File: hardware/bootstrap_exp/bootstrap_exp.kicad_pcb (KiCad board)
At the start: 4 copper layers, 86.4 x 40.6 mm, 32 parts, among them J1 Conn_Coaxial, J2 Conn_01x01, J3 Conn_01x03, J4 Conn_01x03, J5 Conn_Coaxial, U1 OPA810DBV, U2 OPA810DBV, U3 OPA810DBV

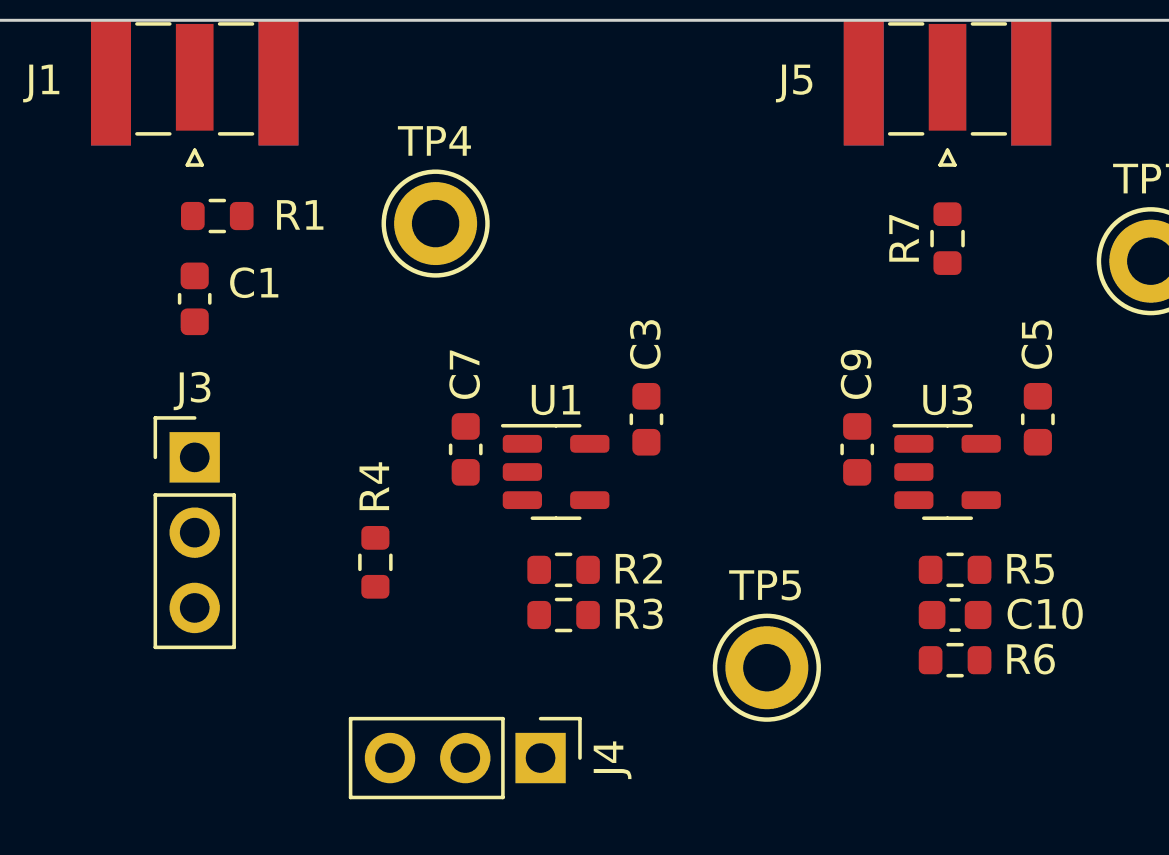
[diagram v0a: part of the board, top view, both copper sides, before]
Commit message: Setup physical stackup and design rules
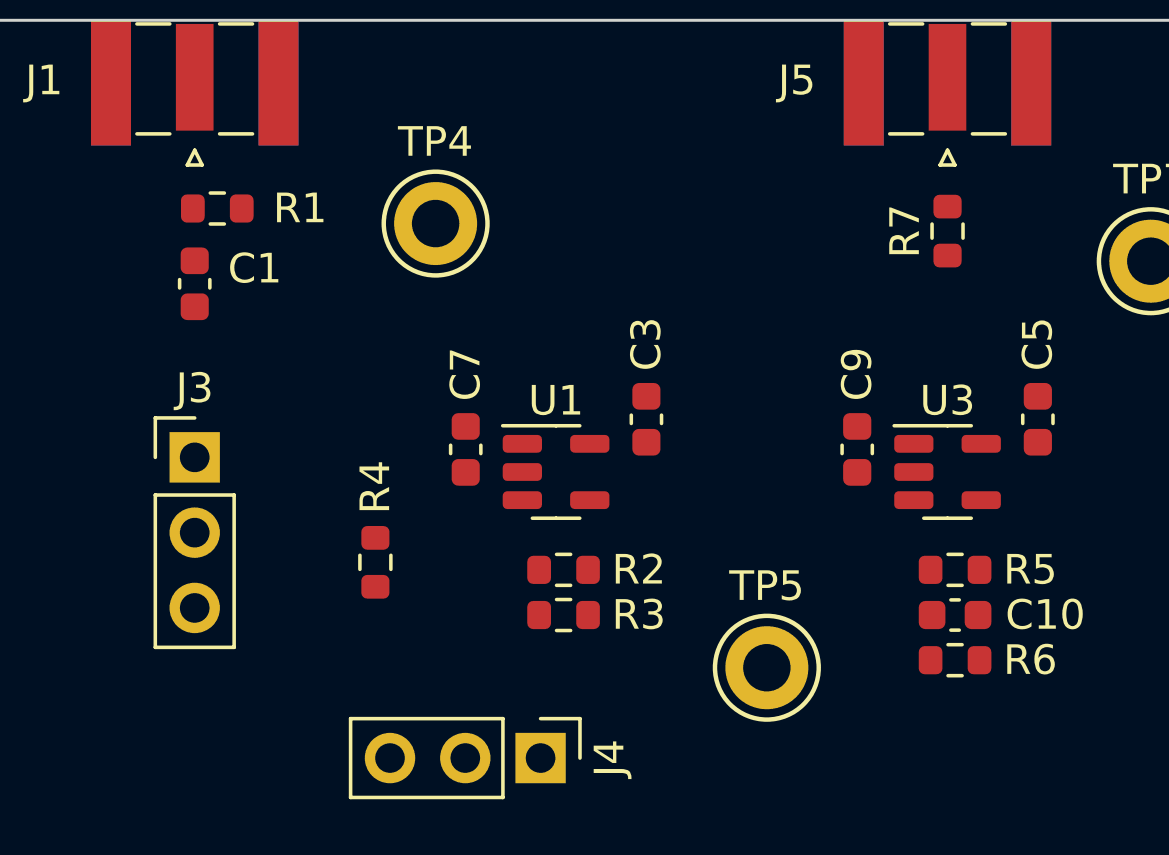
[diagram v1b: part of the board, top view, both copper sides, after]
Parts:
- moved C1 0.51 mm to (129.5, 85.1)
- moved R1 0.25 mm to (130.3, 82.5)
- moved R7 0.25 mm to (154.9, 83.3)
- turned R6 to 180 degrees
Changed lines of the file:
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@@
 (kicad_pcb (version 20211014) (generator pcbnew)
   (general
-    (thickness 4.69)
+    (thickness 1.59)
   )
   (paper "A4")
@@
       (layer "F.Mask" (type "Top Solder Mask") (thickness 0.01))
       (layer "F.Cu" (type "copper") (thickness 0.035))
-      (layer "dielectric 1" (type "core") (thickness 1.51) (material "FR4") (epsilon_r 4.5) (loss_tangent 0.02))
-      (layer "In1.Cu" (type "copper") (thickness 0.035))
-      (layer "dielectric 2" (type "prepreg") (thickness 1.51) (material "FR4") (epsilon_r 4.5) (loss_tangent 0.02))
-      (layer "In2.Cu" (type "copper") (thickness 0.035))
-      (layer "dielectric 3" (type "core") (thickness 1.51) (material "FR4") (epsilon_r 4.5) (loss_tangent 0.02))
+      (layer "dielectric 1" (type "core") (thickness 0.1) (material "FR4") (epsilon_r 4.05) (loss_tangent 0.02))
+      (layer "In1.Cu" (type "copper") (thickness 0.0175))
+      (layer "dielectric 2" (type "prepreg") (thickness 1.265) (material "FR4") (epsilon_r 4.6) (loss_tangent 0.02))
+      (layer "In2.Cu" (type "copper") (thickness 0.0175))
+      (layer "dielectric 3" (type "core") (thickness 0.1) (material "FR4") (epsilon_r 4.05) (loss_tangent 0.02))
       (layer "B.Cu" (type "copper") (thickness 0.035))
       (layer "B.Mask" (type "Bottom Solder Mask") (thickness 0.01))
@@
       (layer "B.SilkS" (type "Bottom Silk Screen"))
       (copper_finish "None")
-      (dielectric_constraints no)
+      (dielectric_constraints yes)
     )
     (pad_to_mask_clearance 0)
@@
   )
   (footprint "Resistor_SMD:R_0603_1608Metric" (layer "F.Cu")
-    (at 155.194 97.79)
+    (at 155.194 97.79 180)
     (descr "Resistor SMD 0603 (1608 Metric), square (rectangular) end terminal, IPC_7351 nominal, (Body size source: IPC-SM-782 page 72, https://www.pcb-3d.com/wordpress/wp-content/uploads/ipc-sm-782a_amendment_1_and_2.pdf), generated with kicad-footprint-generator")
     (tags "resistor")
@@
     (property "Sheetname" "")
     (attr smd)
-    (fp_text reference "R6" (at 2.54 0) (layer "F.SilkS")
+    (fp_text reference "R6" (at -2.54 0) (layer "F.SilkS")
       (effects (font (size 1 1) (thickness 0.15)))
     )
@@
     (fp_line (start 0.8 0.4125) (end -0.8 0.4125) (layer "F.Fab") (width 0.1))
     (fp_line (start -0.8 0.4125) (end -0.8 -0.4125) (layer "F.Fab") (width 0.1))
-    (pad "1" smd roundrect (at -0.825 0) (size 0.8 0.95) (layers "F.Cu" "F.Paste" "F.Mask") (roundrect_rratio 0.25)
+    (pad "1" smd roundrect (at -0.825 0 180) (size 0.8 0.95) (layers "F.Cu" "F.Paste" "F.Mask") (roundrect_rratio 0.25)
       (net 7 "Net-(C10-Pad2)") (pintype "passive"))
-    (pad "2" smd roundrect (at 0.825 0) (size 0.8 0.95) (layers "F.Cu" "F.Paste" "F.Mask") (roundrect_rratio 0.25)
+    (pad "2" smd roundrect (at 0.825 0 180) (size 0.8 0.95) (layers "F.Cu" "F.Paste" "F.Mask") (roundrect_rratio 0.25)
       (net 4 "GND") (pintype "passive"))
     (model "${KICAD6_3DMODEL_DIR}/Resistor_SMD.3dshapes/R_0603_1608Metric.wrl"
@@
   )
   (footprint "Resistor_SMD:R_0603_1608Metric" (layer "F.Cu")
-    (at 130.302 82.804)
+    (at 130.302 82.55)
     (descr "Resistor SMD 0603 (1608 Metric), square (rectangular) end terminal, IPC_7351 nominal, (Body size source: IPC-SM-782 page 72, https://www.pcb-3d.com/wordpress/wp-content/uploads/ipc-sm-782a_amendment_1_and_2.pdf), generated with kicad-footprint-generator")
     (tags "resistor")
@@
   )
   (footprint "Capacitor_SMD:C_0603_1608Metric" (layer "F.Cu")
-    (at 129.54 85.598 90)
+    (at 129.54 85.09 90)
     (descr "Capacitor SMD 0603 (1608 Metric), square (rectangular) end terminal, IPC_7351 nominal, (Body size source: IPC-SM-782 page 76, https://www.pcb-3d.com/wordpress/wp-content/uploads/ipc-sm-782a_amendment_1_and_2.pdf), generated with kicad-footprint-generator")
     (tags "capacitor")
@@
   )
   (footprint "Resistor_SMD:R_0603_1608Metric" (layer "F.Cu")
-    (at 154.94 83.566 90)
+    (at 154.94 83.312 90)
     (descr "Resistor SMD 0603 (1608 Metric), square (rectangular) end terminal, IPC_7351 nominal, (Body size source: IPC-SM-782 page 72, https://www.pcb-3d.com/wordpress/wp-content/uploads/ipc-sm-782a_amendment_1_and_2.pdf), generated with kicad-footprint-generator")
     (tags "resistor")

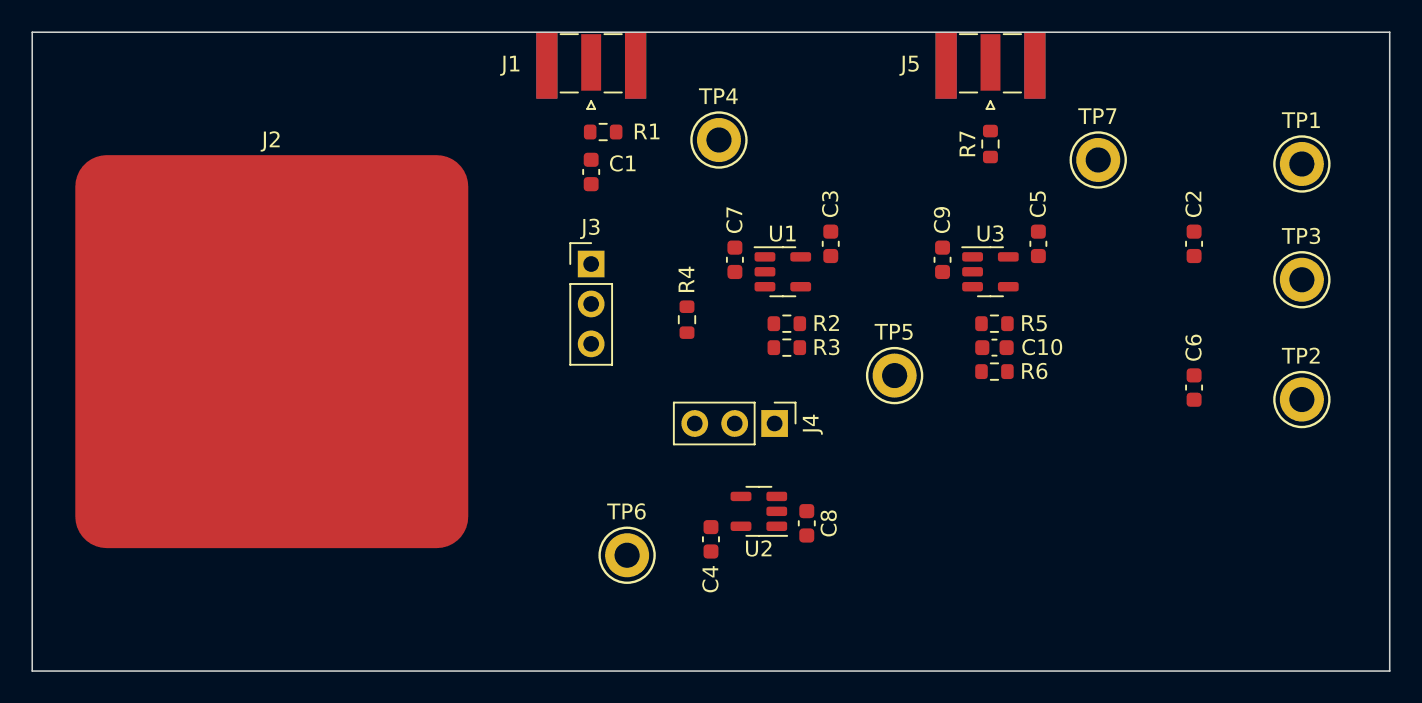
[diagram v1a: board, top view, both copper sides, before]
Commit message: Adjust layout for simplified design
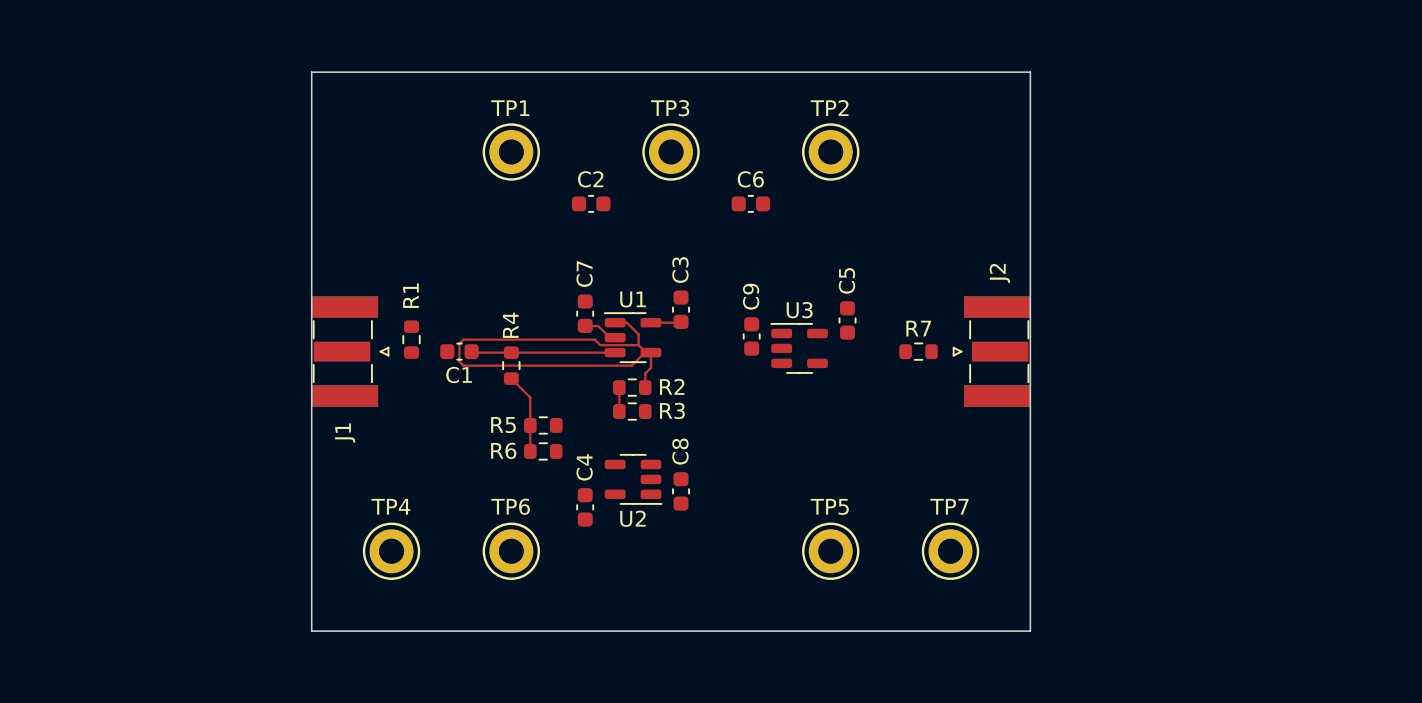
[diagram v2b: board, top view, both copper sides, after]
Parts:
- removed C10: DNI, Capacitor_SMD:C_0603_1608Metric
- removed the J2 at (109.2, 96.5)
- removed J3, J4: Conn_01x03, Connector_PinHeader_2.54mm:PinHeader_1x03_P2.54mm_Vertical
- R5: value 10k -> DNI
- R6: value 100 -> DNI
- moved TP1 50.3 mm to (124.5, 83.8)
- moved TP3 40.9 mm to (134.6, 83.8)
- moved C2 38.4 mm to (129.5, 87.1), turned to 0 degrees
- moved TP2 33.9 mm to (144.8, 83.8)
- moved TP4 33.4 mm to (116.8, 109.2)
- moved C6 30.5 mm to (139.7, 87.1), turned to 180 degrees
- moved R5 29.4 mm to (126.5, 101.2)
- moved R6 29.1 mm to (126.5, 102.9), turned to 0 degrees
- moved TP7 26.6 mm to (152.4, 109.2)
- moved J1 24.0 mm to (113.9, 96.5), turned to -90 degrees
- moved J2 18.2 mm to (155.4, 96.5), turned to 90 degrees
- moved R1 18.0 mm to (118.1, 95.8), turned to 90 degrees
- moved C1 14.2 mm to (121.2, 96.5), turned to 180 degrees
- moved R7 14.0 mm to (150.4, 96.5), turned to 0 degrees
- moved C9 13.1 mm to (139.8, 95.6)
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- renumbered J5 to J2
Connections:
- net /FRONT_OUT renamed Net-(TP5-Pad1)
- C1 pad 1: /SIG_CAP -> Net-(U1-Pad3)
- R2 pad 2: /BOOT_DIV -> Net-(R2-Pad2)
- R3 pad 1: /BOOT_DIV -> Net-(R2-Pad2)
- R4 pad 1: /FRONT_IN -> Net-(U1-Pad3)
- R4 pad 2: /BOOT_V -> Net-(R4-Pad2)
- R5 pad 1: /AMP_OUT -> Net-(R4-Pad2)
- R5 pad 2: Net-(C10-Pad2) -> Net-(R2-Pad2)
- R6 pad 1: Net-(C10-Pad2) -> Net-(R4-Pad2)
- R6 pad 2: GND -> Net-(TP6-Pad1)
- R7 pad 1: /AMP_OUT -> Net-(TP7-Pad1)
- TP4 pad 1: /SIG_CAP -> Net-(U1-Pad3)
- TP6 pad 1: /BOOT_BUF -> Net-(TP6-Pad1)
- TP7 pad 1: /AMP_OUT -> Net-(TP7-Pad1)
- U1 pad 3: /FRONT_IN -> Net-(U1-Pad3)
- U2 pad 1: /BOOT_BUF -> Net-(TP6-Pad1)
- U2 pad 3: /BOOT_DIV -> Net-(R2-Pad2)
- U2 pad 4: /BOOT_BUF -> Net-(TP6-Pad1)
- U3 pad 1: /AMP_OUT -> Net-(TP7-Pad1)
- U3 pad 4: Net-(C10-Pad2) -> Net-(TP7-Pad1)
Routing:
- net Net-(TP5-Pad1): track 0.00 -> 31.3 mm
- net Net-(U1-Pad3): track 0.00 -> 9.26 mm
- net Net-(R4-Pad2): track 0.00 -> 5.14 mm
- net /V-: track 0.00 -> 2.22 mm
- net /V+: track 0.00 -> 1.93 mm
- net Net-(R2-Pad2): track 0.00 -> 1.52 mm
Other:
- board size 86.4 x 40.6 mm -> 45.7 x 35.6 mm

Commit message: Remove test point for bootstrapped high-Z node
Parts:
- removed TP4: ?, TestPoint:TestPoint_Keystone_5005-5009_Compact
- moved TP6 7.62 mm to (116.8, 109.5)
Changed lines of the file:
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@@
-  )
-  (footprint "TestPoint:TestPoint_Keystone_5005-5009_Compact" (layer "F.Cu")
-    (at 116.84 109.22)
-    (descr "Keystone Miniature THM Test Point 5005-5009, http://www.keyelco.com/product-pdf.cfm?p=1314")
-    (tags "Through Hole Mount Test Points")
-    (property "Sheetfile" "bootstrap_exp.kicad_sch")
-    (property "Sheetname" "")
-    (attr through_hole)
-    (fp_text reference "TP4" (at 0 -2.794) (layer "F.SilkS")
-      (effects (font (size 1 1) (thickness 0.15)))
-    )
-    (fp_text value "?" (at 0 3.048) (layer "F.Fab")
-      (effects (font (size 1 1) (thickness 0.15)))
-    )
-    (fp_text user "${REFERENCE}" (at 0 0) (layer "F.Fab")
-      (effects (font (size 0.6 0.6) (thickness 0.09)))
-    )
-    (fp_circle (center 0 0) (end 1.75 0) (layer "F.SilkS") (width 0.15) (fill none))
-    (fp_circle (center 0 0) (end 2 0) (layer "F.CrtYd") (width 0.05) (fill none))
-    (fp_line (start -1.25 0.4) (end -1.25 -0.4) (layer "F.Fab") (width 0.15))
-    (fp_line (start 1.25 0.4) (end -1.25 0.4) (layer "F.Fab") (width 0.15))
-    (fp_line (start -1.25 -0.4) (end 1.25 -0.4) (layer "F.Fab") (width 0.15))
-    (fp_line (start 1.25 -0.4) (end 1.25 0.4) (layer "F.Fab") (width 0.15))
-    (fp_circle (center 0 0) (end 1.6 0) (layer "F.Fab") (width 0.15) (fill none))
-    (pad "1" thru_hole circle (at 0 0) (size 2.8 2.8) (drill 1.6) (layers *.Cu *.Mask)
-      (net 5 "Net-(U1-Pad3)") (pinfunction "1") (pintype "passive"))
-    (model "${KICAD6_3DMODEL_DIR}/TestPoint.3dshapes/TestPoint_Keystone_5005-5009_Compact.wrl"
-      (offset (xyz 0 0 0))
-      (scale (xyz 1 1 1))
-      (rotate (xyz 0 0 0))
-    )
   )
   (footprint "TestPoint:TestPoint_Keystone_5005-5009_Compact" (layer "F.Cu")
@@
   )
   (footprint "TestPoint:TestPoint_Keystone_5005-5009_Compact" (layer "F.Cu")
-    (at 124.46 109.22)
+    (at 116.84 109.474)
     (descr "Keystone Miniature THM Test Point 5005-5009, http://www.keyelco.com/product-pdf.cfm?p=1314")
     (tags "Through Hole Mount Test Points")
